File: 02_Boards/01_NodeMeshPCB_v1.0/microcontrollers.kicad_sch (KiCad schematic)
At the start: 0 parts

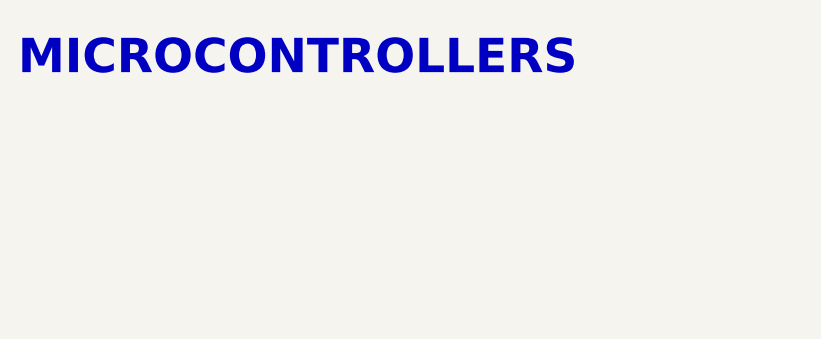
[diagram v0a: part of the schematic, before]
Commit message: 3V3 LDO Schematic
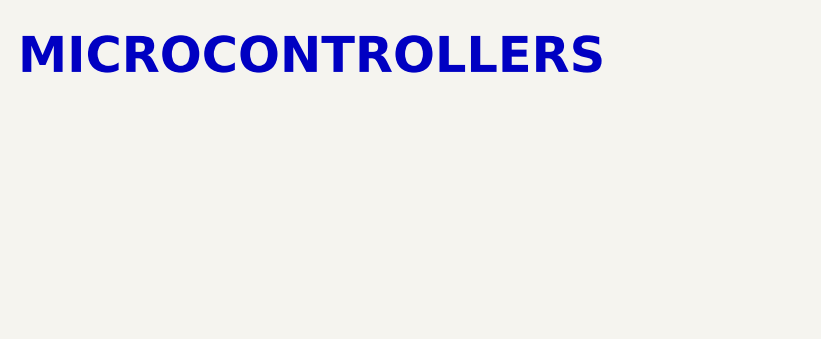
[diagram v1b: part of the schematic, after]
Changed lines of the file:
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@@
 		(effects
 			(font
-				(size 3.81 3.81)
+				(size 4 4)
 				(bold yes)
 			)

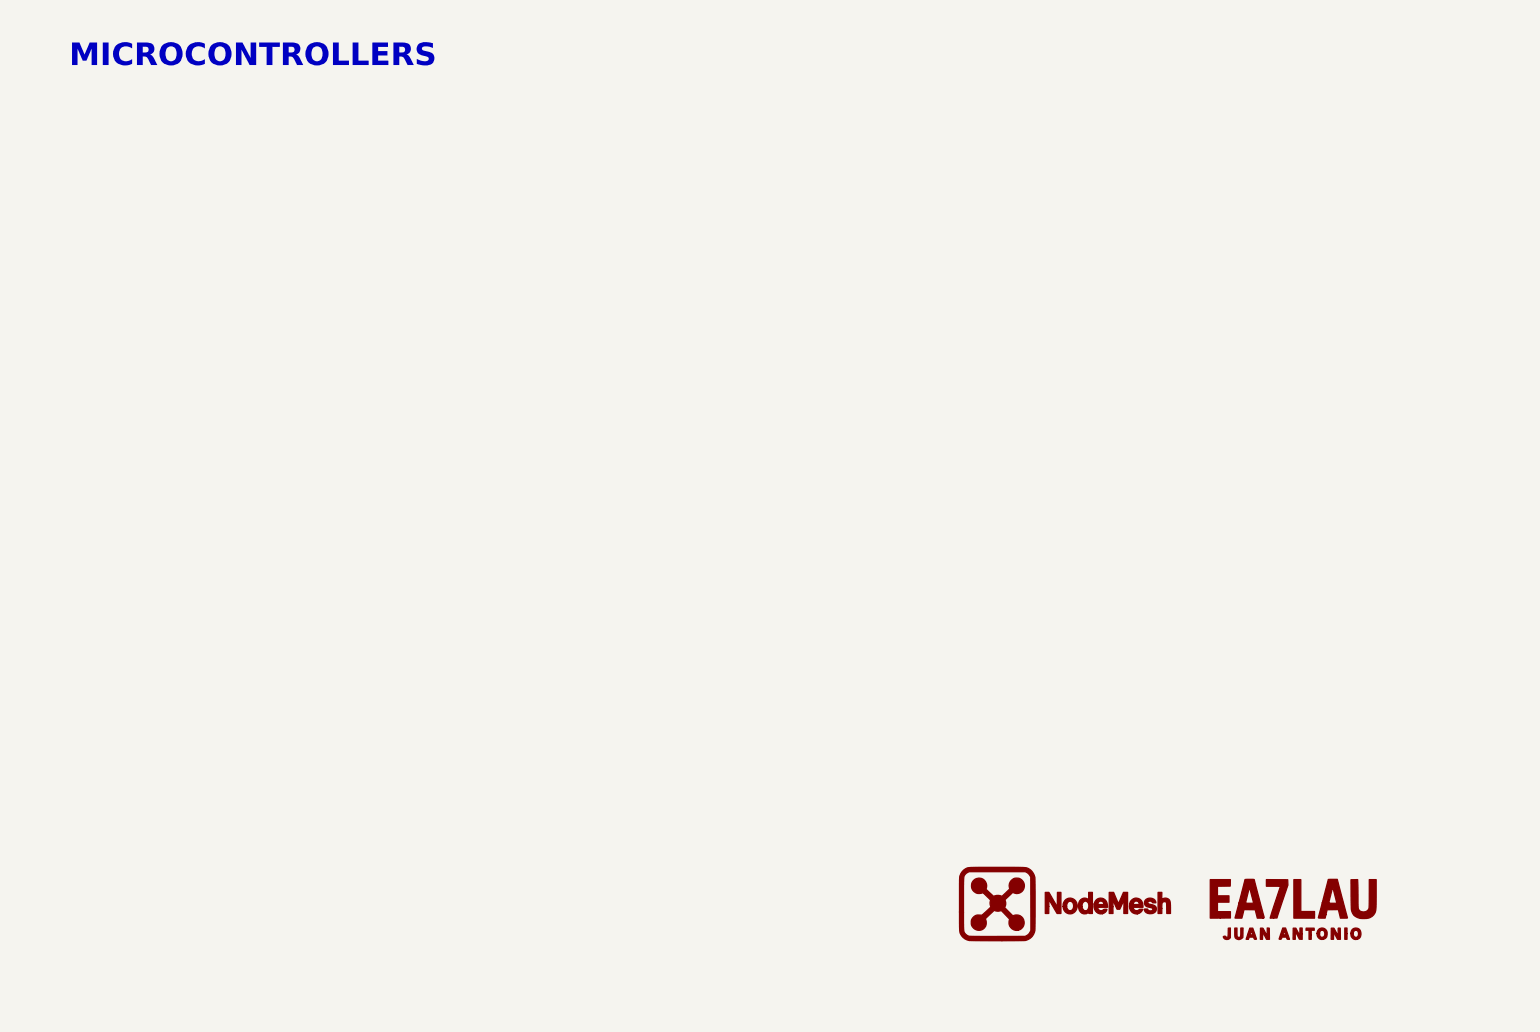
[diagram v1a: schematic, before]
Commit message: firmware project creation
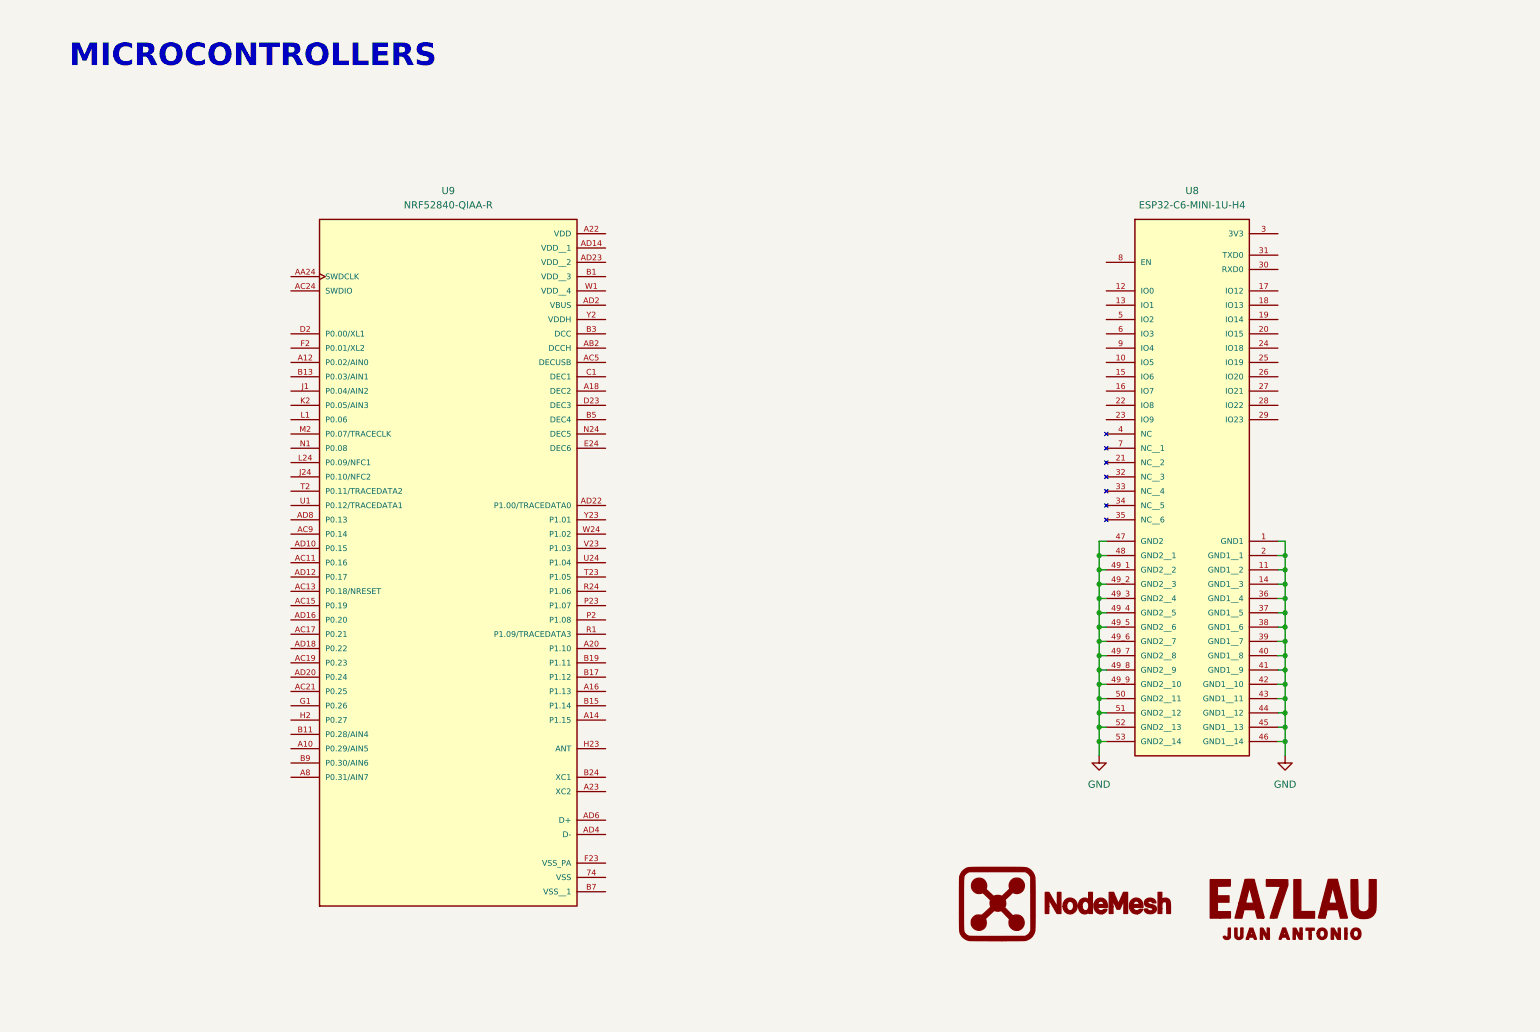
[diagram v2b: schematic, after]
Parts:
- added U8: ESP32-C6-MINI-1U-H4, ESP32-C6-MINI-1U-H4:XCVR_ESP32-C6-MINI-1U-H4, symbol ESP32-C6-MINI-1U-H4:ESP32-C6-MINI-1U-H4
- added U9: NRF52840-QIAA-R, NRF52840-QIAA-R:XCVR_NRF52840-QIAA-R, symbol NRF52840-QIAA-R:NRF52840-QIAA-R
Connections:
- new net GND: U8.1 (GND1), U8.11 (GND1__2), U8.14 (GND1__3), U8.2 (GND1__1), U8.36 (GND1__4), U8.37 (GND1__5), U8.38 (GND1__6), U8.39 (GND1__7), U8.40 (GND1__8), U8.41 (GND1__9), U8.42 (GND1__10), U8.43 (GND1__11), U8.44 (GND1__12), U8.45 (GND1__13), U8.46 (GND1__14), U8.47 (GND2), U8.48 (GND2__1), U8.49_1 (GND2__2), U8.49_2 (GND2__3), U8.49_3 (GND2__4), U8.49_4 (GND2__5), U8.49_5 (GND2__6), U8.49_6 (GND2__7), U8.49_7 (GND2__8), U8.49_8 (GND2__9), U8.49_9 (GND2__10), U8.50 (GND2__11), U8.51 (GND2__12), U8.52 (GND2__13), U8.53 (GND2__14)

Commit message: nRF52840 schematic
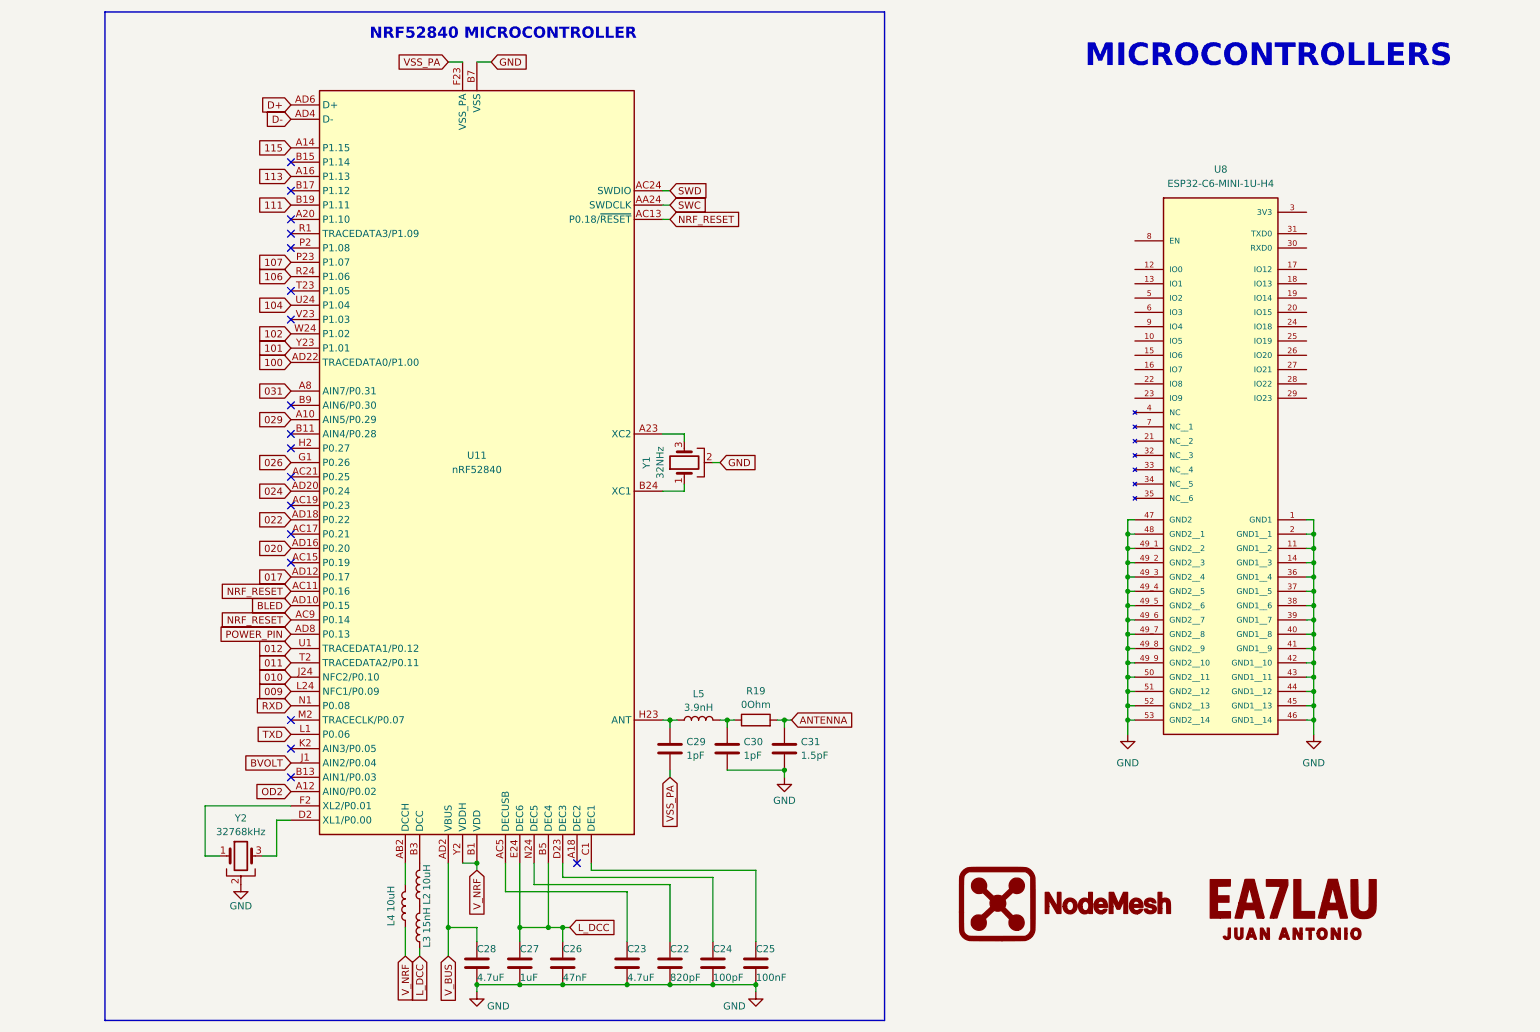
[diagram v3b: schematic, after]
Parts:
- removed U9: NRF52840-QIAA-R, NRF52840-QIAA-R:XCVR_NRF52840-QIAA-R, symbol NRF52840-QIAA-R:NRF52840-QIAA-R
- added C22: 820pF, symbol Device:C
- added C23, C28: 4.7uF, symbol Device:C
- added C24: 100pF, symbol Device:C
- added C25: 100nF, symbol Device:C
- added C26: 47nF, symbol Device:C
- added C27: 1uF, symbol Device:C
- added C29, C30: 1pF, symbol Device:C
- added C31: 1.5pF, symbol Device:C
- added L2, L4: 10uH, symbol Device:L
- added L3: 15nH, symbol Device:L
- added L5: 3.9nH, symbol Device:L
- added R19: 0Ohm, symbol Device:R
- added U11: nRF52840, Package_DFN_QFN:Nordic_AQFN-73-1EP_7x7mm_P0.5mm, symbol MCU_Nordic:nRF52840
- added Y1: 32NHz, symbol Device:Crystal_GND2
- added Y2: 32768kHz, symbol Device:Crystal_GND2
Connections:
- net GND: now also C22.2, C23.2, C24.2, C25.2, C26.2, C27.2, C28.2, C30.2, C31.2, U11.B7 (VSS), U11.EP (VSS), Y1.2, Y2.2
- new net: C25.1, U11.C1 (DEC1)
- new net: C29.1, L5.1, U11.H23 (ANT)
- new net: C30.1, L5.2, R19.1
- new net: C24.1, U11.D23 (DEC3)
- new net: U11.A23 (XC2), Y1.3
- new net: L4.2, U11.AB2 (DCCH)
- new net: C23.1, U11.AC5 (DECUSB)
- new net: U11.B24 (XC1), Y1.1
- new net: L2.2, U11.B3 (DCC)
- new net: U11.D2 (XL1/P0.00), Y2.3
- new net: U11.F2 (XL2/P0.01), Y2.1
- new net: C22.1, U11.N24 (DEC5)
- new net: L2.1, L3.2
- new net 009: U11.L24 (NFC1/P0.09)
- new net 010: U11.J24 (NFC2/P0.10)
- new net 011: U11.T2 (TRACEDATA2/P0.11)
- new net 012: U11.U1 (TRACEDATA1/P0.12)
- new net 017: U11.AD12 (P0.17)
- new net 020: U11.AD16 (P0.20)
- new net 022: U11.AD18 (P0.22)
- new net 024: U11.AD20 (P0.24)
- new net 026: U11.G1 (P0.26)
- new net 029: U11.A10 (AIN5/P0.29)
- new net 031: U11.A8 (AIN7/P0.31)
- new net 100: U11.AD22 (TRACEDATA0/P1.00)
- new net 101: U11.Y23 (P1.01)
- new net 102: U11.W24 (P1.02)
- new net 104: U11.U24 (P1.04)
- new net 106: U11.R24 (P1.06)
- new net 107: U11.P23 (P1.07)
- new net 111: U11.B19 (P1.11)
- new net 113: U11.A16 (P1.13)
- new net 115: U11.A14 (P1.15)
- new net ANTENNA: C31.1, R19.2
- new net BLED: U11.AD10 (P0.15)
- new net BVOLT: U11.J1 (AIN2/P0.04)
- new net D+: U11.AD6 (D+)
- new net D-: U11.AD4 (D-)
- new net L_DCC: C26.1, C27.1, L3.1, U11.B5 (DEC4), U11.E24 (DEC6)
- new net NRF_RESET: U11.AC11 (P0.16), U11.AC13 (P0.18/~{RESET}), U11.AC9 (P0.14)
- new net OD2: U11.A12 (AIN0/P0.02)
- new net POWER_PIN: U11.AD8 (P0.13)
- new net RXD: U11.N1 (P0.08)
- new net SWC: U11.AA24 (SWDCLK)
- new net SWD: U11.AC24 (SWDIO)
- new net TXD: U11.L1 (P0.06)
- new net VSS_PA: C29.2, U11.F23 (VSS_PA)
- new net V_BUS: C28.1, U11.AD2 (VBUS)
- new net V_NRF: L4.1, U11.A22 (VDD), U11.AD14 (VDD), U11.AD23 (VDD), U11.B1 (VDD), U11.W1 (VDD), U11.Y2 (VDDH)
- no-connect marks 0 -> 18
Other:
- note added: "NRF52840 MICROCONTROLLER"
- moved on the sheet: U8

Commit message: PCB placement
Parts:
- removed Y2: 32768kHz, symbol Device:Crystal_GND2
- added C21, C22, C26, C27: 100nF, Capacitor_SMD:C_0603_1608Metric, symbol Device:C
- added D5: Blue, LED_SMD:LED_0603_1608Metric, symbol Device:LED
- added J3: USB4145-03-0070-C_REVA2, 01_Footprints:USB4145-03-0070-C, symbol USB4145-03-0070-C:USB4145-03-0070-C_REVA2
- added J4: 61300411121, 01_Footprints:61300411121, symbol 61300411121:61300411121
- added J5: SMA-J-P-H-ST-TH1, 01_Footprints:SMA-J-P-H-ST-TH1, symbol SMA-J-P-H-ST-TH1:SMA-J-P-H-ST-TH1
- added Q4: NDS355AN, 01_Footprints:NDS355AN, symbol NDS355AN:NDS355AN
- added R10, R11: 0Ohm, Resistor_SMD:R_0603_1608Metric, symbol Device:R
- added R12, R13, R14, R16, R17: 100kOhm, Resistor_SMD:R_0603_1608Metric, symbol Device:R
- added R18: 1kOhm, Resistor_SMD:R_0603_1608Metric, symbol Device:R
- added R19, R20: 10kOhm, Resistor_SMD:R_0603_1608Metric, symbol Device:R
- added R9: 5.1kOhm, Resistor_SMD:R_0603_1608Metric, symbol Device:R
- added SW1, SW2, SW3, SW4: B3U-1000P, Button_Switch_SMD:SW_SPST_B3U-1000P, symbol Switch:SW_Push
- added Y2: FC-12M_32.7680KA-A3, 01_Footprints:FC-12M_327680KA-A3, symbol FC-12M_327680KA-A3:FC-12M_32.7680KA-A3
- C23: renamed from C29; footprint (none) -> Capacitor_SMD:C_0603_1608Metric
- C24: renamed from C30; footprint (none) -> Capacitor_SMD:C_0603_1608Metric
- C25: renamed from C31; footprint (none) -> Capacitor_SMD:C_0603_1608Metric
- C28: footprint (none) -> Capacitor_SMD:C_0603_1608Metric
- C29: renamed from C27; footprint (none) -> Capacitor_SMD:C_0603_1608Metric
- C30: renamed from C26; footprint (none) -> Capacitor_SMD:C_0603_1608Metric
- C31: renamed from C23; footprint (none) -> Capacitor_SMD:C_0603_1608Metric
- C32: renamed from C22; footprint (none) -> Capacitor_SMD:C_0603_1608Metric
- C33: renamed from C24; footprint (none) -> Capacitor_SMD:C_0603_1608Metric
- C34: renamed from C25; footprint (none) -> Capacitor_SMD:C_0603_1608Metric
- L2: renamed from L5; footprint (none) -> Inductor_SMD:L_0603_1608Metric
- L3: renamed from L2; footprint (none) -> Inductor_SMD:L_0603_1608Metric
- L4: footprint (none) -> Inductor_SMD:L_0603_1608Metric
- L5: renamed from L3; footprint (none) -> Inductor_SMD:L_0603_1608Metric
- R15: renamed from R19; footprint (none) -> Resistor_SMD:R_0603_1608Metric
- U5: renamed from U8; footprint ESP32-C6-MINI-1U-H4:XCVR_ESP32-C6-MINI-1U-H4 -> 01_Footprints:ESP32-C6-MINI-1U-H4
- Y1: value 32NHz -> 32MHz XRCGB32M000F3M00R0; footprint (none) -> 01_Footprints:XRCGB32M000F3M00R0
- renumbered U11 to U6
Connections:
- net BLED: now also D5.2 (A)
- net D+: now also J3.A6 (DP1)
- net D-: now also J3.A7 (DN1)
- net GND: now also C21.2, C22.2, C26.2, C27.2, J3.A1 (GND_A), J3.A12 (GND_A), J4.1, J5.G1, J5.G2, J5.G3, J5.G4, Q4.2, R13.2, R18.1, R9.2, SW1.2, SW2.2, SW3.2, SW4.2
- net NRF_RESET: now also C21.1, Q4.3, R12.1, SW1.1
- net RXD: now also U5.30 (RXD0), J4.3; no longer U6.N1 (P0.08)
- net TXD: now also U5.31 (TXD0), J4.2; no longer U6.L1 (P0.06)
- net V_BUS: now also J3.A4 (VBUS_A), J3.A9 (VBUS_A)
- net V_NRF: now also R12.2, R14.2
- net at U6.D2 (XL1/P0.00): now also Y2.2
- net at U6.F2 (XL2/P0.01): now also Y2.1
- net CRTL_RESET: now reaches U5.19 (IO14)
- net CRTL_RESET: now also Q4.1, R13.1
- net IO9: now reaches U5.23 (IO9)
- net IO9: now also C27.1, R17.2, SW4.1
- net at U5.27 (IO21): now also R10.2
- net at U5.28 (IO22): now also R11.2
- net V_SYS: now reaches U5.3 (3V3)
- net V_SYS: now also J4.4, R16.2, R17.1, R19.1, R20.1
- net EN: now reaches U5.8 (EN)
- net EN: now also C26.1, R16.1, SW3.1
- net 009 renamed LR_RST
- net 010 renamed LR_DIO1
- net 011 renamed SCL
- net SCL: now also R11.1, R20.2
- net 012: no longer names the net of U6.U1 (TRACEDATA1/P0.12)
- net 017 renamed LR_RXEN
- net 020 renamed GPS_RX
- net 022 renamed GPS_TX
- net 024: no longer names the net of U6.AD20 (P0.24)
- net 026: no longer names the net of U6.G1 (P0.26)
- net 029 renamed LR_BUSY
- net 031: no longer names the net of U6.A8 (AIN7/P0.31)
- net 100 renamed PRG_BTN
- net PRG_BTN: now also C22.1, R14.1, SW2.1
- net 101: no longer names the net of U6.Y23 (P1.01)
- net 102: no longer names the net of U6.W24 (P1.02)
- net 104 renamed SDA
- net SDA: now also R10.1, R19.2
- net 106: no longer names the net of U6.R24 (P1.06)
- net 107: no longer names the net of U6.P23 (P1.07)
- net 111 renamed SCK
- net 113 renamed NSS
- net 115 renamed MOSI
- net ANTENNA: no longer names the net of C25.1, R15.2
- net ANTENNA: now also J5.1
- net BVOLT: no longer names the net of U6.J1 (AIN2/P0.04)
- net OD2 renamed MISO
- net POWER_PIN: no longer names the net of U6.AD8 (P0.13)
- net SWC: no longer names the net of U6.AA24 (SWDCLK)
- net SWD: no longer names the net of U6.AC24 (SWDIO)
- new net: J3.A5 (CC1), R9.1
- new net: J3.B1 (GND_B), J3.B12 (GND_B)
- new net: J3.B4 (VBUS_B), J3.B9 (VBUS_B)
- new net: J3.S1 (SHIELD), J3.S2 (SHIELD), J3.S3 (SHIELD), J3.S4 (SHIELD)
- new net: D5.1 (K), R18.2
- new net CRTL_OUT_1: U6.N1 (P0.08)
- new net PWR_CRTL_GPS: U6.L1 (P0.06)
- no-connect marks 18 -> 61
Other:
- note added: "BLE ANTENNA"
- note added: "ESP32 PROG IF"
- note added: "ESP32 RESET AND BOOT BUTTONS"
- note added: "ESP32-C6-MINI-1U-H4"
- note added: "LED INDICATOR"
- note added: "NRF52840 BOOT BOTTON"
- note added: "NRF52840 RESET CIRCUIT"
- note added: "POWER I2C"
- note added: "USBC CONNECTOR"
- note added: "WATCH-DOG MICROCONTROLLER"
- moved on the sheet: C23, C24, C25, C28, C29, C30, C31, C32, C33, C34, L2, L3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
